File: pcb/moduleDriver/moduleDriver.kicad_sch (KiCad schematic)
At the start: 44 parts, among them J1 MOTOR, J10 Sensor, J11 Power, J12 Power, J13 Power, J14 LOOPBACK, J2 MOTOR, J3 MOTOR, J4 MOTOR, J5 IDC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

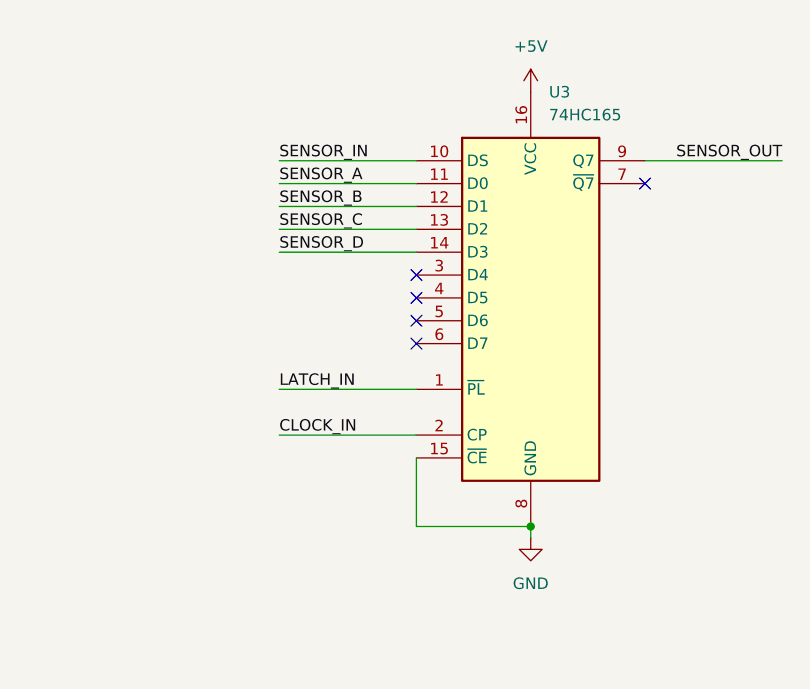
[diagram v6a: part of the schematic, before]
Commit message: Reduce traces on ground plane
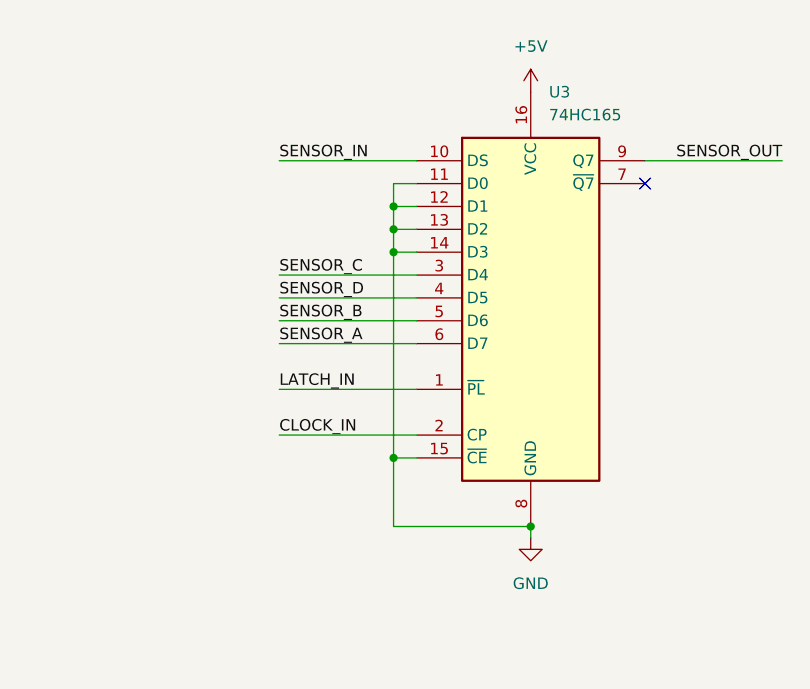
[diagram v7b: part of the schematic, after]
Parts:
- H1, H2, H3: footprint MountingHole:MountingHole_3.2mm_M3_ISO7380_Pad -> MountingHole:MountingHole_3.2mm_M3_ISO7380
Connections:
- net GND: now also U3.11 (D0), U3.12 (D1), U3.13 (D2), U3.14 (D3)
- net SENSOR_A: now also U3.6 (D7); no longer U3.11 (D0)
- net SENSOR_B: now also U3.5 (D6); no longer U3.12 (D1)
- net SENSOR_C: now also U3.3 (D4); no longer U3.13 (D2)
- net SENSOR_D: now also U3.4 (D5); no longer U3.14 (D3)
- no-connect marks 38 -> 34
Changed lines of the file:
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@@
     (rev "0.2")
   )
+  (junction (at 294.64 58.42) (diameter 0) (color 0 0 0 0)
+  )
   (junction (at 374.65 64.77) (diameter 0) (color 0 0 0 0)
   )
@@
   (junction (at 372.11 53.34) (diameter 0) (color 0 0 0 0)
   )
+  (junction (at 294.64 55.88) (diameter 0) (color 0 0 0 0)
+  )
+  (junction (at 294.64 83.82) (diameter 0) (color 0 0 0 0)
+  )
   (junction (at 156.21 41.91) (diameter 0) (color 0 0 0 0)
   )
@@
   )
   (junction (at 374.65 78.74) (diameter 0) (color 0 0 0 0)
+  )
+  (junction (at 294.64 60.96) (diameter 0) (color 0 0 0 0)
   )
   (junction (at 364.49 59.69) (diameter 0) (color 0 0 0 0)
@@
   (no_connect (at 45.72 102.87))
   (no_connect (at 45.72 138.43))
-  (no_connect (at 297.18 68.58))
   (no_connect (at 74.93 184.15))
   (no_connect (at 54.61 194.31))
@@
   (no_connect (at 66.04 153.67))
   (no_connect (at 45.72 123.19))
-  (no_connect (at 297.18 66.04))
   (no_connect (at 45.72 113.03))
   (no_connect (at 45.72 125.73))
   (no_connect (at 81.28 100.33))
-  (no_connect (at 297.18 71.12))
   (no_connect (at 81.28 118.11))
   (no_connect (at 63.5 153.67))
@@
   (no_connect (at 60.96 153.67))
   (no_connect (at 45.72 107.95))
-  (no_connect (at 297.18 63.5))
   (no_connect (at 45.72 115.57))
   (no_connect (at 45.72 140.97))
@@
     (stroke (width 0) (type default) (color 0 0 0 0))
   )
+  (wire (pts (xy 294.64 60.96) (xy 294.64 83.82))
+    (stroke (width 0) (type default) (color 0 0 0 0))
+  )
   (wire (pts (xy 196.85 203.2) (xy 196.85 209.55))
     (stroke (width 0) (type default) (color 0 0 0 0))
@@
     (stroke (width 0) (type default) (color 0 0 0 0))
   )
+  (wire (pts (xy 294.64 53.34) (xy 294.64 55.88))
+    (stroke (width 0) (type default) (color 0 0 0 0))
+  )
+  (wire (pts (xy 294.64 83.82) (xy 297.18 83.82))
+    (stroke (width 0) (type default) (color 0 0 0 0))
+  )
   (wire (pts (xy 49.53 226.06) (xy 49.53 228.6))
     (stroke (width 0) (type default) (color 0 0 0 0))
   )
-  (wire (pts (xy 297.18 83.82) (xy 297.18 91.44))
+  (wire (pts (xy 294.64 83.82) (xy 294.64 91.44))
     (stroke (width 0) (type default) (color 0 0 0 0))
   )
@@
     (stroke (width 0) (type default) (color 0 0 0 0))
   )
-  (wire (pts (xy 281.94 60.96) (xy 297.18 60.96))
+  (wire (pts (xy 281.94 66.04) (xy 297.18 66.04))
     (stroke (width 0) (type default) (color 0 0 0 0))
   )
@@
     (stroke (width 0) (type default) (color 0 0 0 0))
   )
+  (wire (pts (xy 281.94 68.58) (xy 297.18 68.58))
+    (stroke (width 0) (type default) (color 0 0 0 0))
+  )
   (wire (pts (xy 91.44 105.41) (xy 97.79 105.41))
     (stroke (width 0) (type default) (color 0 0 0 0))
@@
     (stroke (width 0) (type default) (color 0 0 0 0))
   )
-  (wire (pts (xy 297.18 91.44) (xy 309.88 91.44))
+  (wire (pts (xy 294.64 91.44) (xy 309.88 91.44))
     (stroke (width 0) (type default) (color 0 0 0 0))
   )
@@
     (stroke (width 0) (type default) (color 0 0 0 0))
   )
+  (wire (pts (xy 294.64 55.88) (xy 294.64 58.42))
+    (stroke (width 0) (type default) (color 0 0 0 0))
+  )
   (wire (pts (xy 224.79 139.7) (xy 247.65 139.7))
     (stroke (width 0) (type default) (color 0 0 0 0))
@@
     (stroke (width 0) (type default) (color 0 0 0 0))
   )
-  (wire (pts (xy 281.94 58.42) (xy 297.18 58.42))
+  (wire (pts (xy 281.94 63.5) (xy 297.18 63.5))
     (stroke (width 0) (type default) (color 0 0 0 0))
   )
@@
     (stroke (width 0) (type default) (color 0 0 0 0))
   )
+  (wire (pts (xy 294.64 58.42) (xy 294.64 60.96))
+    (stroke (width 0) (type default) (color 0 0 0 0))
+  )
   (wire (pts (xy 41.91 118.11) (xy 41.91 130.81))
     (stroke (width 0) (type default) (color 0 0 0 0))
@@
     (stroke (width 0) (type default) (color 0 0 0 0))
   )
+  (wire (pts (xy 294.64 58.42) (xy 297.18 58.42))
+    (stroke (width 0) (type default) (color 0 0 0 0))
+  )
   (wire (pts (xy 85.09 105.41) (xy 85.09 130.81))
     (stroke (width 0) (type default) (color 0 0 0 0))
@@
     (stroke (width 0) (type default) (color 0 0 0 0))
   )
+  (wire (pts (xy 297.18 53.34) (xy 294.64 53.34))
+    (stroke (width 0) (type default) (color 0 0 0 0))
+  )
   (wire (pts (xy 30.48 189.23) (xy 54.61 189.23))
     (stroke (width 0) (type default) (color 0 0 0 0))
@@
     (stroke (width 0) (type default) (color 0 0 0 0))
   )
-  (wire (pts (xy 281.94 55.88) (xy 297.18 55.88))
+  (wire (pts (xy 281.94 71.12) (xy 297.18 71.12))
     (stroke (width 0) (type default) (color 0 0 0 0))
   )
@@
     (stroke (width 0) (type default) (color 0 0 0 0))
   )
+  (wire (pts (xy 294.64 60.96) (xy 297.18 60.96))
+    (stroke (width 0) (type default) (color 0 0 0 0))
+  )
   (wire (pts (xy 364.49 82.55) (xy 364.49 81.28))
     (stroke (width 0) (type default) (color 0 0 0 0))
@@
     (stroke (width 0) (type default) (color 0 0 0 0))
   )
+  (wire (pts (xy 294.64 55.88) (xy 297.18 55.88))
+    (stroke (width 0) (type default) (color 0 0 0 0))
+  )
   (wire (pts (xy 201.93 59.69) (xy 212.09 59.69))
     (stroke (width 0) (type default) (color 0 0 0 0))
@@
   )
   (wire (pts (xy 147.32 185.42) (xy 170.18 185.42))
-    (stroke (width 0) (type default) (color 0 0 0 0))
-  )
-  (wire (pts (xy 281.94 53.34) (xy 297.18 53.34))
     (stroke (width 0) (type default) (color 0 0 0 0))
   )
@@
     (effects (font (size 1.27 1.27)) (justify left bottom))
   )
-  (label "SENSOR_D" (at 281.94 60.96 0)
+  (label "SENSOR_D" (at 281.94 66.04 0)
     (effects (font (size 1.27 1.27)) (justify left bottom))
   )
@@
     (effects (font (size 1.27 1.27)) (justify left bottom))
   )
-  (label "SENSOR_A" (at 281.94 53.34 0)
-    (effects (font (size 1.27 1.27)) (justify left bottom))
-  )
-  (label "SENSOR_B" (at 281.94 55.88 0)
+  (label "SENSOR_A" (at 281.94 71.12 0)
+    (effects (font (size 1.27 1.27)) (justify left bottom))
+  )
+  (label "SENSOR_B" (at 281.94 68.58 0)
     (effects (font (size 1.27 1.27)) (justify left bottom))
   )
@@
     (effects (font (size 1.27 1.27)) (justify left bottom))
   )
-  (label "SENSOR_C" (at 281.94 58.42 0)
+  (label "SENSOR_C" (at 281.94 63.5 0)
     (effects (font (size 1.27 1.27)) (justify left bottom))
   )
@@
       (effects (font (size 1.27 1.27)) (justify left))
     )
-    (property "Footprint" "MountingHole:MountingHole_3.2mm_M3_ISO7380_Pad" (id 2) (at 365.76 135.89 0)
+    (property "Footprint" "MountingHole:MountingHole_3.2mm_M3_ISO7380" (id 2) (at 365.76 135.89 0)
       (effects (font (size 1.27 1.27)) hide)
     )
@@
       (effects (font (size 1.27 1.27)) (justify left))
     )
-    (property "Footprint" "MountingHole:MountingHole_3.2mm_M3_ISO7380_Pad" (id 2) (at 365.76 130.81 0)
+    (property "Footprint" "MountingHole:MountingHole_3.2mm_M3_ISO7380" (id 2) (at 365.76 130.81 0)
       (effects (font (size 1.27 1.27)) hide)
     )
@@
       (effects (font (size 1.27 1.27)) (justify left))
     )
-    (property "Footprint" "MountingHole:MountingHole_3.2mm_M3_ISO7380_Pad" (id 2) (at 365.76 140.97 0)
+    (property "Footprint" "MountingHole:MountingHole_3.2mm_M3_ISO7380" (id 2) (at 365.76 140.97 0)
       (effects (font (size 1.27 1.27)) hide)
     )
@@
     )
     (path "/720a37ec-5a11-4ea1-b384-42b6706cc10c"
-      (reference "H1") (unit 1) (value "MountingHole") (footprint "MountingHole:MountingHole_3.2mm_M3_ISO7380_Pad")
+      (reference "H1") (unit 1) (value "MountingHole") (footprint "MountingHole:MountingHole_3.2mm_M3_ISO7380")
     )
     (path "/6f964950-0372-4ba1-9fab-17d5b9fe1f15"
-      (reference "H2") (unit 1) (value "MountingHole") (footprint "MountingHole:MountingHole_3.2mm_M3_ISO7380_Pad")
+      (reference "H2") (unit 1) (value "MountingHole") (footprint "MountingHole:MountingHole_3.2mm_M3_ISO7380")
     )
     (path "/ada26385-a60b-45ef-94cb-e7206725bdb7"
-      (reference "H3") (unit 1) (value "MountingHole") (footprint "MountingHole:MountingHole_3.2mm_M3_ISO7380_Pad")
+      (reference "H3") (unit 1) (value "MountingHole") (footprint "MountingHole:MountingHole_3.2mm_M3_ISO7380")
     )
     (path "/2dab68f6-502c-477d-a7bb-0fcaf664652e"

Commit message: Add LCSC part numbers
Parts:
- C1: LCSC# (none) -> C176665
- C2, C3, C5, C6: LCSC# (none) -> C108343
- C4: LCSC# (none) -> C134721
- D1, D2, D3: LCSC# (none) -> NCD0603R1
- R1: value 220R -> 100R; LCSC# (none) -> C100700
- R10: LCSC# (none) -> C269690
- R11: LCSC# (none) -> C3017736
- R2, R3: value 220R -> 30R; LCSC# (none) -> C170726
- R4: LCSC# (none) -> C22936
- R5, R6, R7, R8: LCSC# (none) -> C881902
- R9: LCSC# (none) -> C166926
- U1, U2: LCSC# (none) -> C7094
- U3: LCSC# (none) -> C5613
- U4: LCSC# (none) -> C5598
- U7: LCSC# (none) -> C7531
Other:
- note added: "Led NCD0603R1 Forward Voltage 2V R = (5V-2V)/0.01A = 30 Ohms R = (12V-2V)/0.01A = 100 Ohms"
